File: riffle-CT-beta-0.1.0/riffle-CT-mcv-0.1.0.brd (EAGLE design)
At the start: 38.7 x 18 mm, 32 parts, among them IC1 MCP3221, IC5 TPS60400DBV

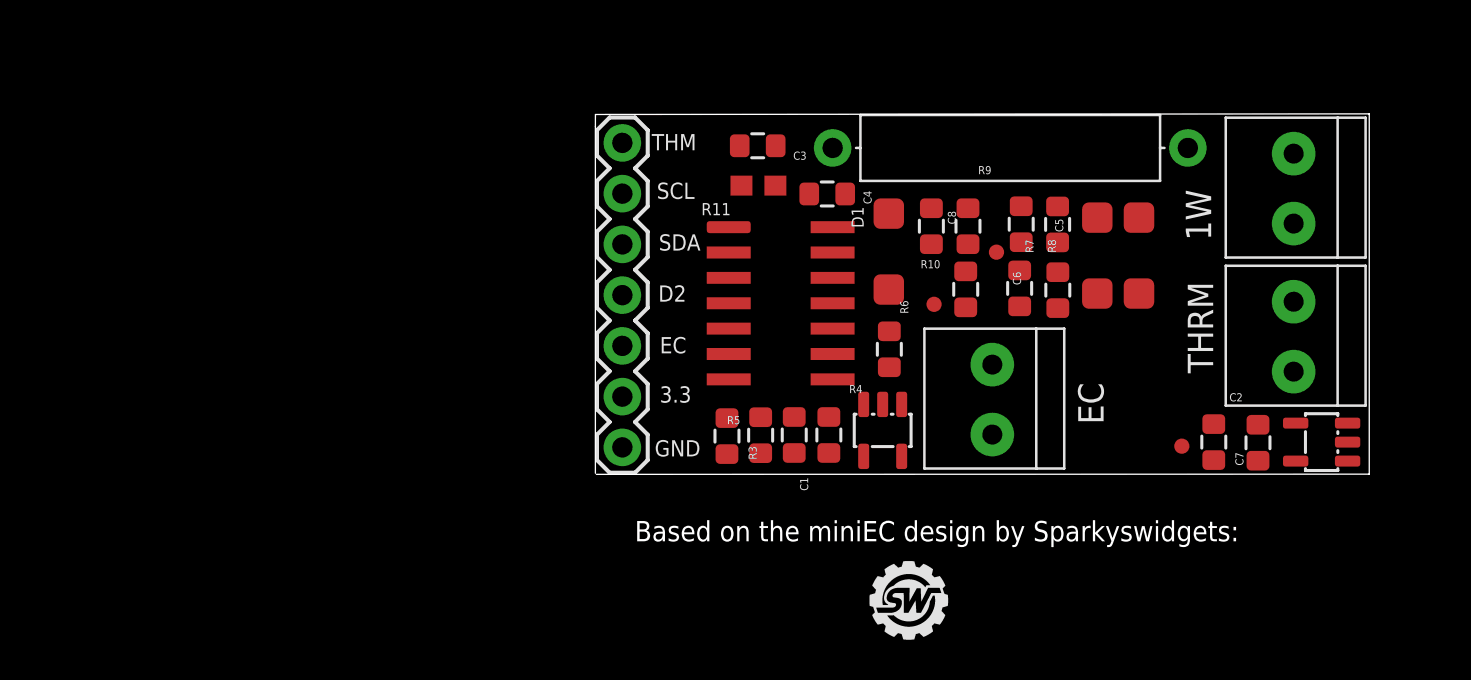
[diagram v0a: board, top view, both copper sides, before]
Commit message: optimized layout of parts
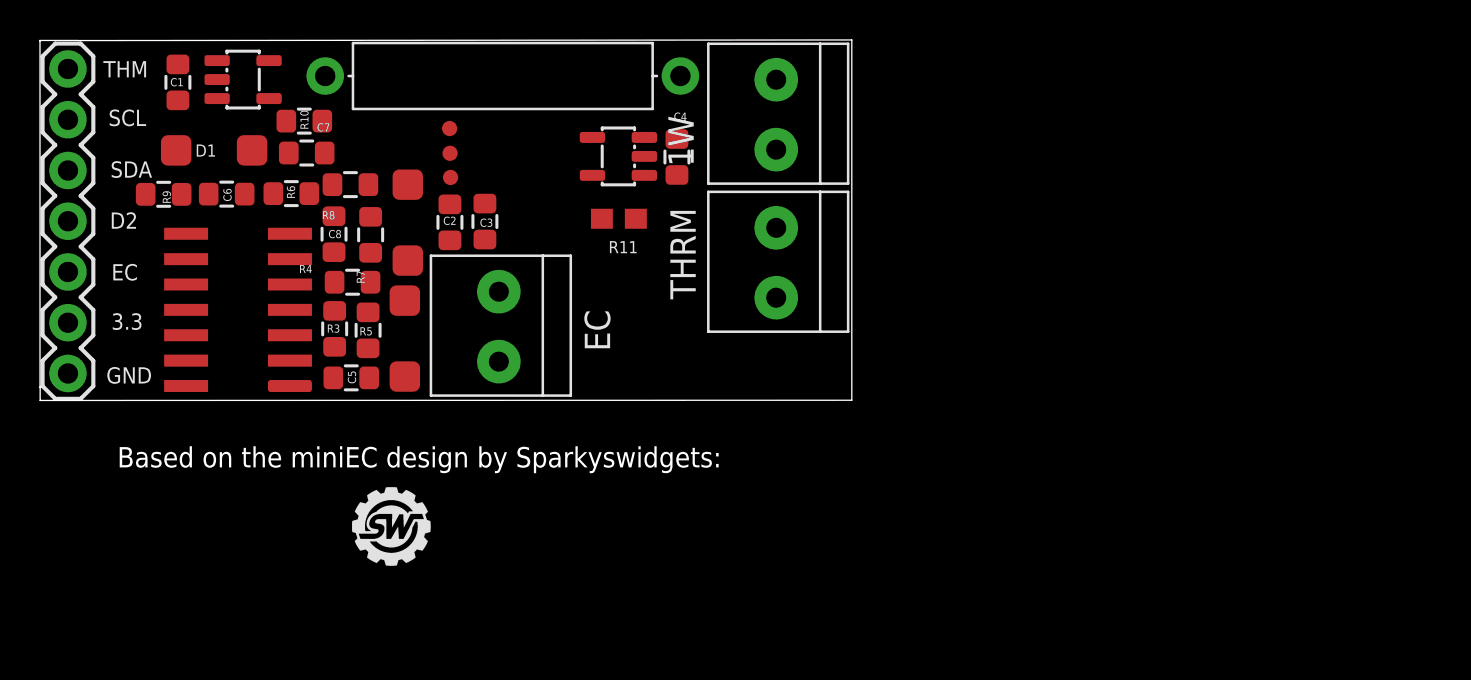
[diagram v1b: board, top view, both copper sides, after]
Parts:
- moved C7 47.7 mm to (13.0, 21.5), turned to 180 degrees
- moved C2 41.9 mm to (20.2, 18.1), turned to 90 degrees
- moved C6 41.9 mm to (8.98, 19.5), turned to 180 degrees
- moved R9 40.3 mm to (5.82, 19.5), turned to 0 degrees
- moved TP2 40.0 mm to (20.1, 22.8)
- moved IC5 38.0 mm to (28.6, 21.4)
- moved D3 36.6 mm to (18.0, 18.1)
- moved IC1 36.5 mm to (9.80, 25.2), turned to 270 degrees
- moved C5 36.2 mm to (15.2, 10.3), turned to 180 degrees
- moved C1 35.5 mm to (6.54, 25.1)
- moved D2 34.9 mm to (17.9, 12.2), turned to 270 degrees
- moved R10 34.2 mm to (12.9, 23.1), turned to 180 degrees
- moved D1 34.1 mm to (8.35, 21.7), turned to 180 degrees
- moved R8 33.6 mm to (15.2, 20.0), turned to 180 degrees
- moved R7 32.6 mm to (16.2, 17.4), turned to 90 degrees
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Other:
- board size 38.7 x 18 mm -> 40.6 x 18 mm

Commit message: optimized layout of parts
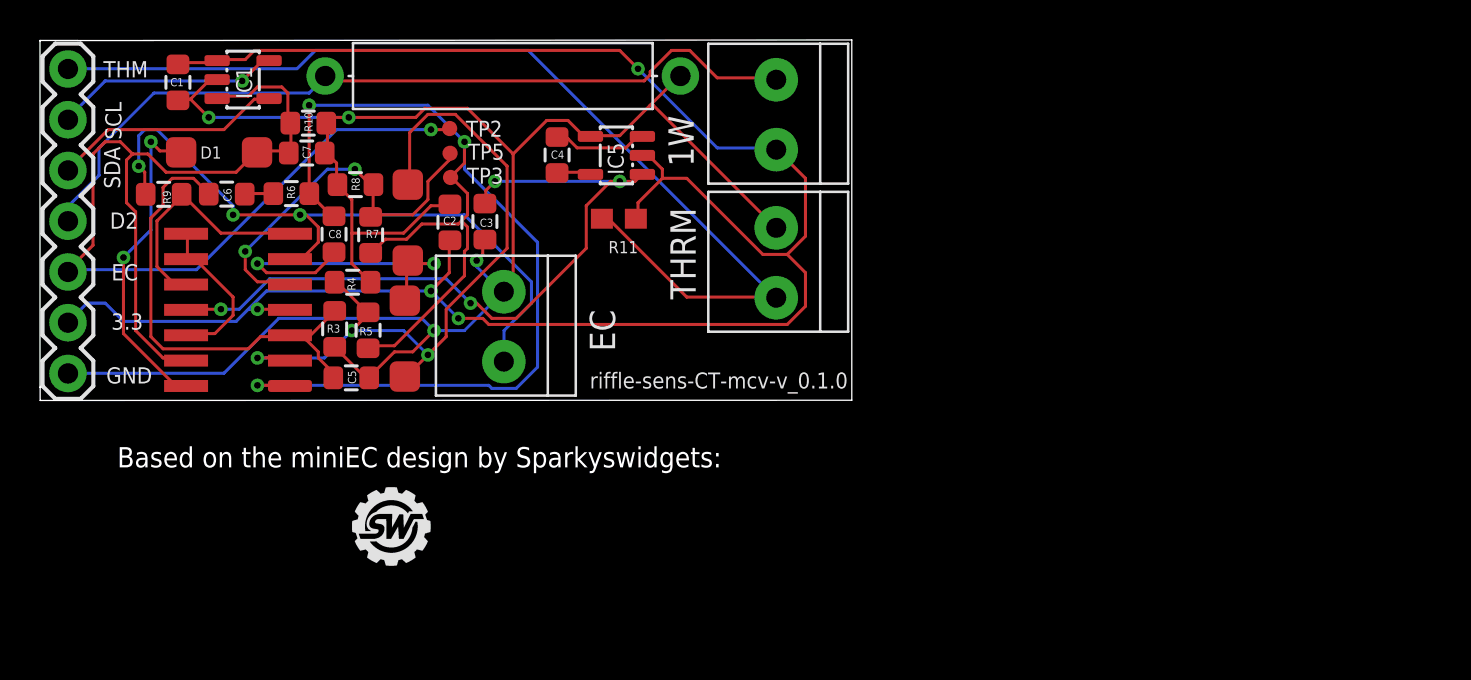
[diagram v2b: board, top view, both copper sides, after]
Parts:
- moved C4 6.00 mm to (25.5, 21.4)
- moved D1 0.27 mm to (8.60, 21.6)
- moved EC 0.25 mm to (22.9, 12.8)
- moved R8 0.25 mm to (15.4, 20.0)
- moved R10 0.22 mm to (13.1, 23.0)
- moved IC5 0.11 mm to (28.5, 21.4)
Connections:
- removed net EC: JP6.5
- net ECVOUT: now also JP6.5
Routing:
- net V+: track 0.00 -> 98.1 mm, vias 0 -> 4
- net GND: track 0.00 -> 96.6 mm, vias 0 -> 4
- net N$33: track 0.00 -> 62.9 mm, vias 0 -> 3
- net ECVOUT: track 0.00 -> 59.1 mm, vias 0 -> 1
- net THRM: track 0.00 -> 51.3 mm
- net D2: track 0.00 -> 41.2 mm
- net N$31: track 0.00 -> 36.6 mm, vias 0 -> 3
- net V-: track 0.00 -> 36.1 mm, vias 0 -> 4
- net N$35: track 0.00 -> 34.6 mm, vias 0 -> 3
- net N$30: track 0.00 -> 24.3 mm
- net N$34: track 0.00 -> 19.5 mm, vias 0 -> 2
- net N$1: track 0.00 -> 16.8 mm, vias 0 -> 2
- net N$41: track 0.00 -> 16.1 mm, vias 0 -> 2
- net N$36: track 0.00 -> 12.2 mm
- net SDA: track 0.00 -> 11.6 mm
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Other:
- board text added: "CERN OHL v 1.2"
- board text added: "IC1"
- board text added: "IC5"
- board text added: "TP2"
- board text added: "TP3"
- board text added: "TP5"
- board text added: "publiclab.org/wiki/riffle"
- board text added: "riffle-sens-CT-mcv-v_0.1.0"

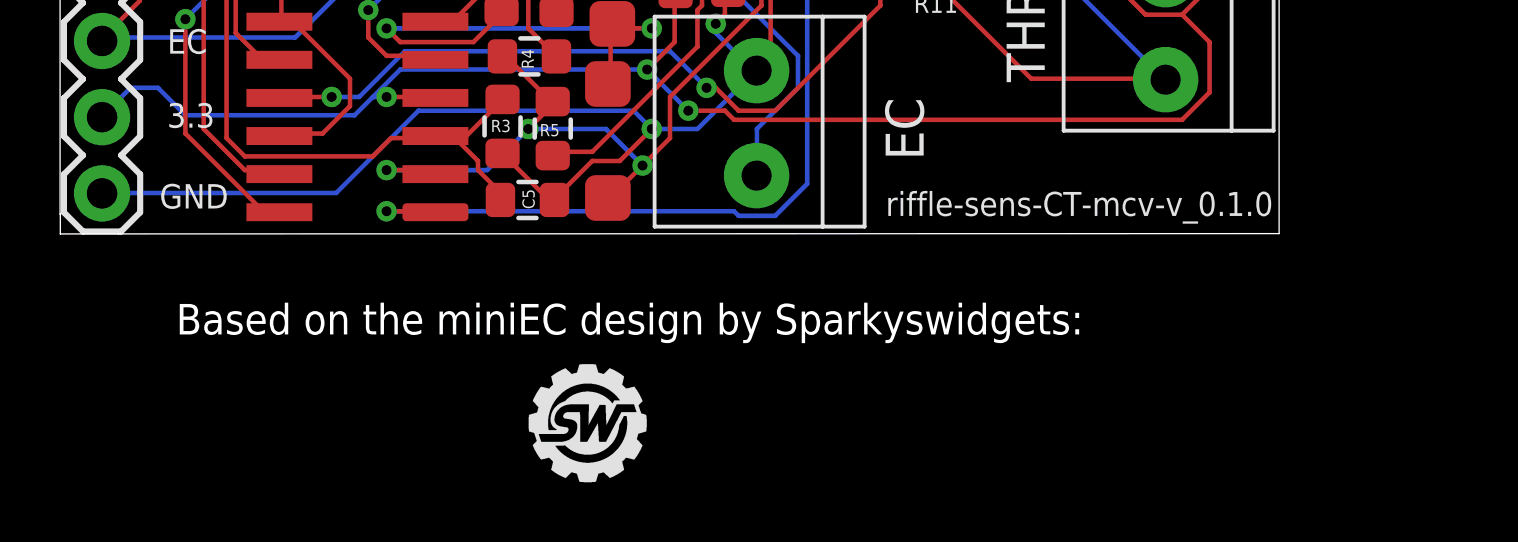
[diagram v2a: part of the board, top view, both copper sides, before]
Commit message: optimized layout of parts
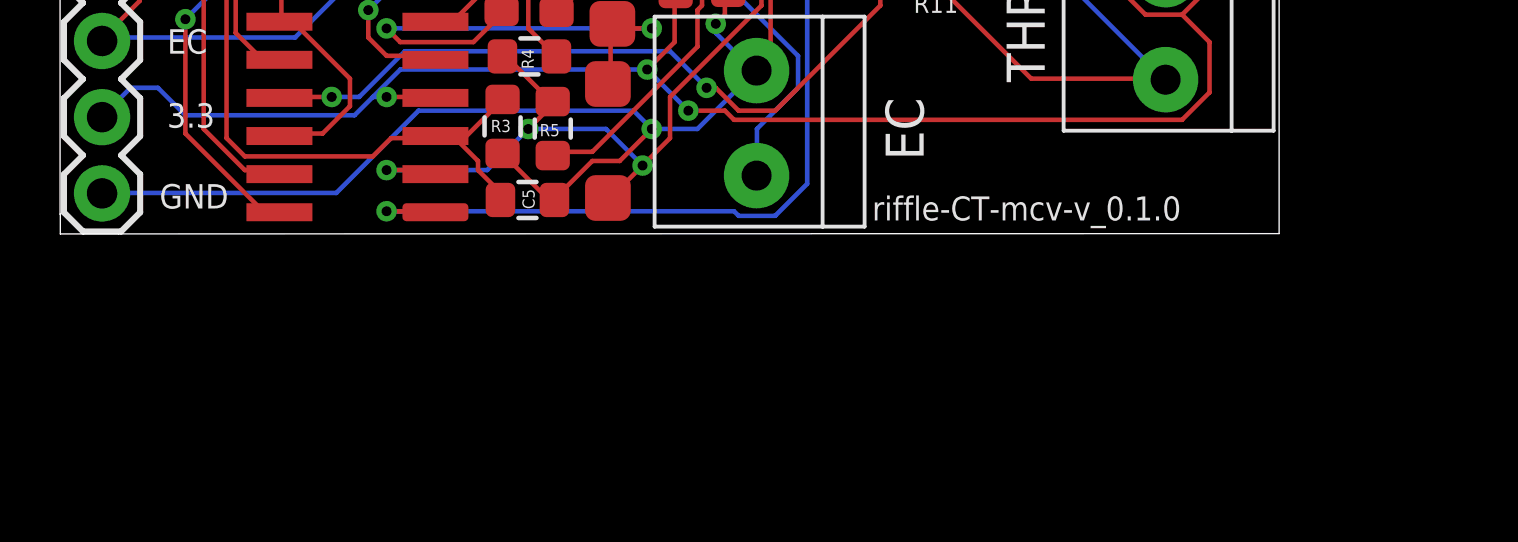
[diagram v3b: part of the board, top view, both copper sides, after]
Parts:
- removed U$4: FRAME_MINIEC, SW_ArtWork:SWPCBLOGOWITHINFO
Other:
- board text added: "riffle-CT-mcv-v_0.1.0"
- board text removed: "Based on the miniEC design by Sparkyswidgets:"
- board text removed: "riffle-sens-CT-mcv-v_0.1.0"
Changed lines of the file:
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@@
 <text x="2.807" y="25.322" size="0.8128" layer="21" font="vector">THM</text>
 <text x="5.247" y="10.811" size="0.8128" layer="21" font="vector" rot="R180">GND</text>
-<text x="3.5" y="5.8" size="1.016" layer="20">Based on the miniEC design by Sparkyswidgets:</text>
 <wire x1="1.53" y1="27.17" x2="-0.37" y2="27.17" width="0" layer="20"/>
 <wire x1="-0.37" y1="27.17" x2="-0.37" y2="27.15" width="0" layer="20"/>
@@
 <text x="10.25" y="24.25" size="0.8" layer="21" rot="R90">IC1</text>
 <text x="28.85" y="20.45" size="0.8" layer="21" rot="R90">IC5</text>
-<text x="27.15" y="9.75" size="0.8" layer="21">riffle-sens-CT-mcv-v_0.1.0</text>
-<text x="27.9" y="25" size="0.8" layer="22" rot="MR0">publiclab.org/wiki/riffle</text>
-<text x="31.65" y="21.75" size="0.8" layer="22" rot="MR0">CERN OHL v 1.2</text>
+<text x="26.7" y="9.6" size="0.8" layer="21" font="vector">riffle-CT-mcv-v_0.1.0</text>
+<text x="31.35" y="23.55" size="0.8" layer="22" font="vector" rot="MR0">publiclab.org/wiki/riffle</text>
+<text x="27.15" y="25.15" size="0.8" layer="22" font="vector" rot="MR0">CERN OHL v 1.2</text>
 </plain>
 <attributes>
@@
 <attribute name="NAME" x="27.15" y="13.694" size="1.27" layer="25" rot="R270"/>
 </element>
-<element name="U$4" library="SW_ArtWork" package="SWPCBLOGOWITHINFO" value="FRAME_MINIEC" x="15.256" y="0.876">
-<attribute name="URL1" value="/portfolio-item/miniEc/" x="15.256" y="0.876" size="0.6096" layer="27" display="off"/>
-<attribute name="URLHOME" value="http://www.sparkyswidgets.com" x="15.256" y="0.876" size="0.6096" layer="27" display="off"/>
-<attribute name="URLPROJECT" value="http://www.sparkyswidgets.com" x="15.256" y="0.876" size="0.6096" layer="27" display="off"/>
-<attribute name="PROJECT" value="Mini eC I2C eC Interface" x="15.256" y="0.876" size="0.6096" layer="27" display="off"/>
-</element>
 </elements>
